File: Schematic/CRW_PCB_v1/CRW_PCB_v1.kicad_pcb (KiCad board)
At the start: 2 copper layers, 114.3 x 38.1 mm, 79 parts, among them Q1 Q_PMOS_GSD, Q2 Q_PMOS_GSD, Q3 Q_NMOS_GSD, Q4 Q_NMOS_GSD, U1 TPS62051DGS, U2 TPS62051DGS, U3 DRV8838DSGR, U4 DRV8838DSGR, U5 DRV8838DSGR

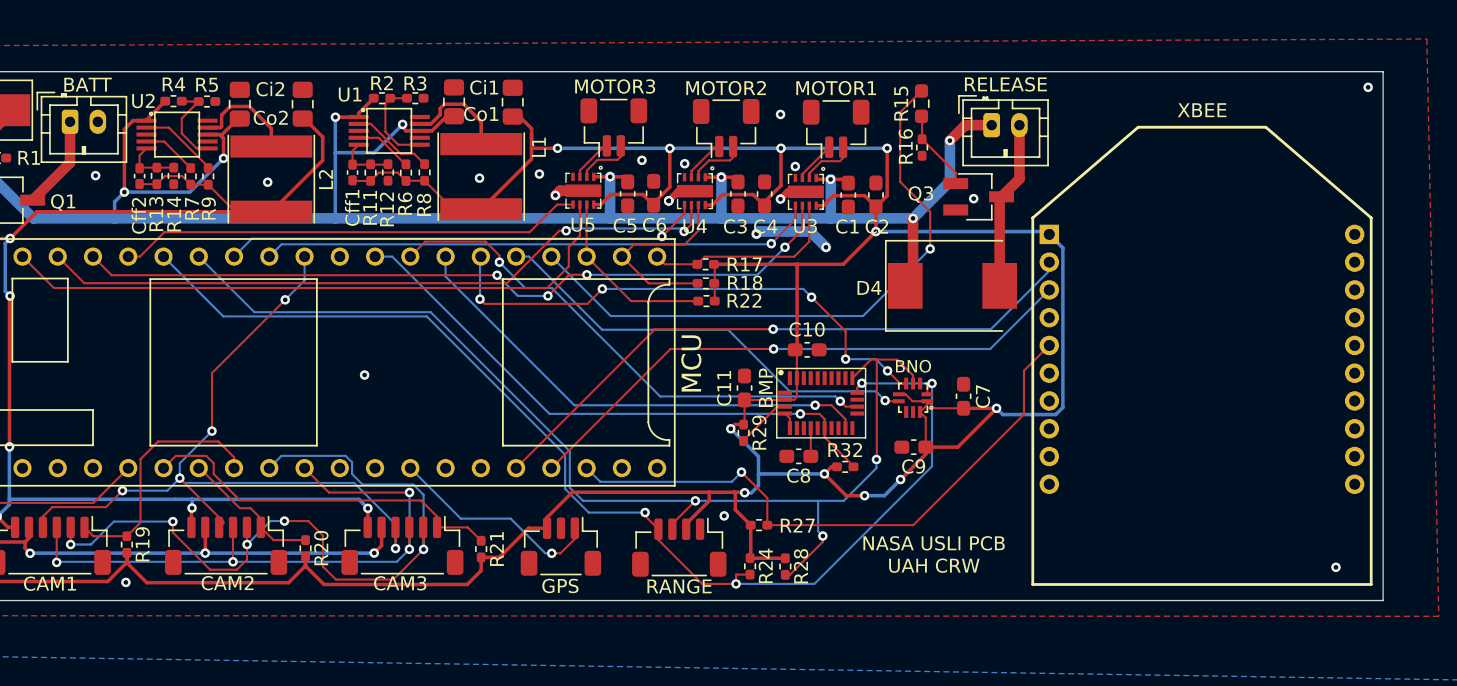
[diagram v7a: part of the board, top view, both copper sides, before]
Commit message: Added Hotwire Connection
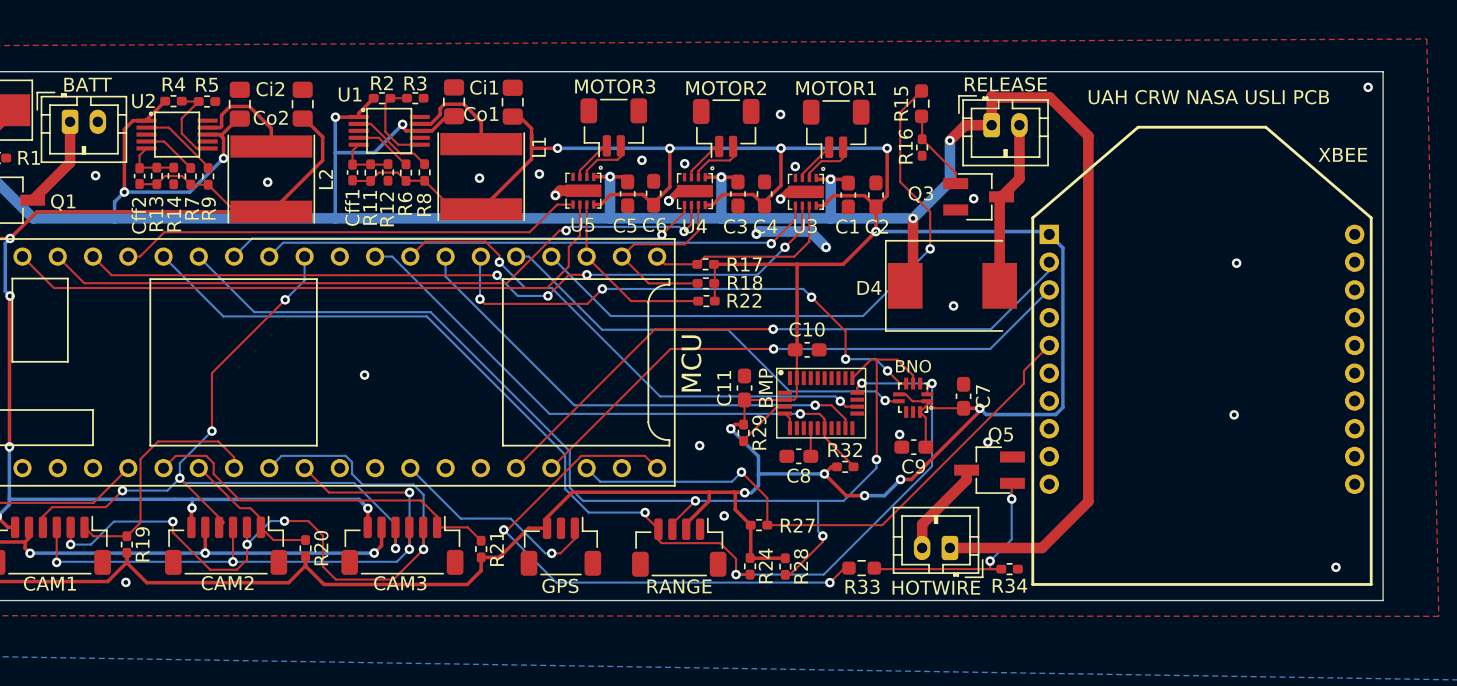
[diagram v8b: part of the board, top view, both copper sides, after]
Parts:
- added HOTWIRE: HOTWIRE, Connector_JST:JST_PH_B2B-PH-K_1x02_P2.00mm_Vertical, F.Cu at (108.5, 59.7)
- added Q5: Q_NMOS_GSD, Package_TO_SOT_SMD:SC-59_Handsoldering, F.Cu at (111.3, 54.1)
- added R33: 220, Resistor_SMD:R_0603_1608Metric_Pad0.98x0.95mm_HandSolder, F.Cu at (102.1, 61.2)
- added R34: 10k, Resistor_SMD:R_0402_1005Metric_Pad0.72x0.64mm_HandSolder, F.Cu at (112.8, 61.2)
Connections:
- MCU pad D32: Net-(MCU1-PadD32) -> HOTWIRE
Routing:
- net +BATT: track 160.9 -> 208.8 mm
- net HOTWIRE: track 0.00 -> 40.5 mm, vias 0 -> 2
- net Net-(Q5-Pad1): track 0.00 -> 16.8 mm, vias 0 -> 2
- net Net-(HOTWIRE1-Pad2): track 0.00 -> 6.93 mm
- net +3V3: track 265.3 -> 263.9 mm
- net XBEE_~RESET: track 44.0 -> 42.7 mm
- net I2C_SCL: track 85.1 -> 84.6 mm
- net -BATT: vias 24 -> 30
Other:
- board text added: "Design: v2"
- board text added: "UAH CRW NASA USLI PCB"
- board text removed: "Design: v1"
